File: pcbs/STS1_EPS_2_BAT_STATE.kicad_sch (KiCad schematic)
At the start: 10 parts, among them U4 MIC841H, U5 MIC841L

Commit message: Intermediate commit.
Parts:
- U5: value MIC841L -> MIC841H
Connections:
- net GND: now also U5.2 (GND)
- net GNDREF: no longer U5.2 (GND)
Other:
- note added: "This implements a hysteresis. At BAT_RAW <= 5V, UVLO_SIGNAL is pulled low. If BAT_RAW increases above >= 5,3V, UVLO_SIGNAL is pulled high."
- note removed: "This implements a hysteresis. At BAT_RAW <= 5V, UVLO_SIGNAL is pulled high. If BAT_RAW increases above >= 5,3V, UVLO_SIGNAL is pulled low."
- moved on the sheet: R31, R33, R35, R36, U5

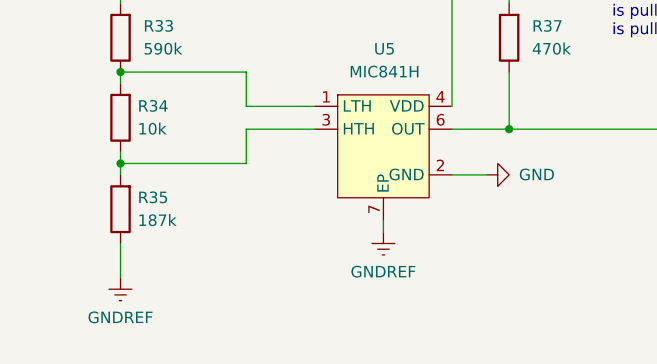
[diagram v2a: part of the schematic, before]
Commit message: Fixed warnings and errors.
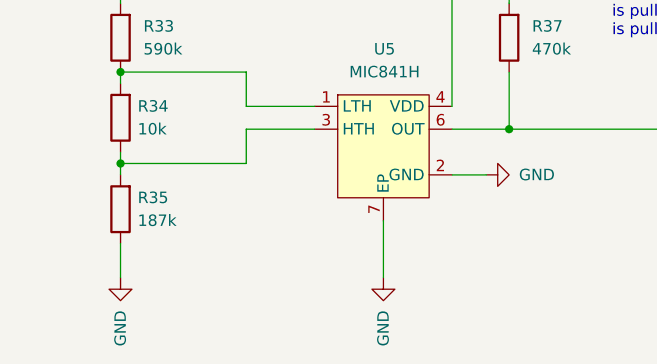
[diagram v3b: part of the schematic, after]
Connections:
- net GNDREF is gone; now on net GND: R35.1, U5.7 (EP)
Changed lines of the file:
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@@
 	(wire
 		(pts
-			(xy 58.42 125.73) (xy 58.42 127)
+			(xy 58.42 125.73) (xy 58.42 132.08)
 		)
 		(stroke
@@
 			)
 			(justify right)
+		)
+	)
+	(symbol
+		(lib_id "power:GND")
+		(at 58.42 132.08 0)
+		(unit 1)
+		(exclude_from_sim no)
+		(in_bom yes)
+		(on_board yes)
+		(dnp no)
+		(property "Reference" "#PWR059"
+			(at 58.42 138.43 0)
+			(effects
+				(font
+					(size 1.27 1.27)
+				)
+				(hide yes)
+			)
+		)
+		(property "Value" "GND"
+			(at 58.42 139.7 90)
+			(effects
+				(font
+					(size 1.27 1.27)
+				)
+				(justify left)
+			)
+		)
+		(property "Footprint" ""
+			(at 58.42 132.08 0)
+			(effects
+				(font
+					(size 1.27 1.27)
+				)
+				(hide yes)
+			)
+		)
+		(property "Datasheet" ""
+			(at 58.42 132.08 0)
+			(effects
+				(font
+					(size 1.27 1.27)
+				)
+				(hide yes)
+			)
+		)
+		(property "Description" "Power symbol creates a global label with name \"GND\" , ground"
+			(at 58.42 132.08 0)
+			(effects
+				(font
+					(size 1.27 1.27)
+				)
+				(hide yes)
+			)
+		)
+		(pin "1"
+		)
+		(instances
+			(project "STS1_EPS_2"
+				(path "/38c03ff7-ea47-4d00-b37d-ddcaa7d87722/f6013889-7b77-4458-9ae4-3903f8947363"
+					(reference "#PWR059")
+					(unit 1)
+				)
+			)
 		)
 	)
@@
 	)
 	(symbol
-		(lib_id "power:GNDREF")
+		(lib_id "power:GND")
 		(at 29.21 132.08 0)
 		(unit 1)
@@
 		(on_board yes)
 		(dnp no)
-		(fields_autoplaced yes)
 		(property "Reference" "#PWR056"
 			(at 29.21 138.43 0)
@@
 			)
 		)
-		(property "Value" "GNDREF"
-			(at 29.21 136.525 0)
-			(effects
-				(font
-					(size 1.27 1.27)
-				)
+		(property "Value" "GND"
+			(at 29.21 139.7 90)
+			(effects
+				(font
+					(size 1.27 1.27)
+				)
+				(justify left)
 			)
 		)
@@
 			)
 		)
-		(property "Description" ""
+		(property "Description" "Power symbol creates a global label with name \"GND\" , ground"
 			(at 29.21 132.08 0)
 			(effects
@@
 					(unit 1)
 				)
-			)
-		)
-	)
-	(symbol
-		(lib_id "power:GNDREF")
-		(at 58.42 127 0)
-		(unit 1)
-		(exclude_from_sim no)
-		(in_bom yes)
-		(on_board yes)
-		(dnp no)
-		(fields_autoplaced yes)
-		(property "Reference" "#PWR059"
-			(at 58.42 133.35 0)
-			(effects
-				(font
-					(size 1.27 1.27)
-				)
-				(hide yes)
-			)
-		)
-		(property "Value" "GNDREF"
-			(at 58.42 131.445 0)
-			(effects
-				(font
-					(size 1.27 1.27)
-				)
-			)
-		)
-		(property "Footprint" ""
-			(at 58.42 127 0)
-			(effects
-				(font
-					(size 1.27 1.27)
-				)
-				(hide yes)
-			)
-		)
-		(property "Datasheet" ""
-			(at 58.42 127 0)
-			(effects
-				(font
-					(size 1.27 1.27)
-				)
-				(hide yes)
-			)
-		)
-		(property "Description" ""
-			(at 58.42 127 0)
-			(effects
-				(font
-					(size 1.27 1.27)
-				)
-				(hide yes)
-			)
-		)
-		(pin "1"
-		)
-		(instances
-			(project "STS1_EPS_2"
-				(path "/38c03ff7-ea47-4d00-b37d-ddcaa7d87722/f6013889-7b77-4458-9ae4-3903f8947363"
-					(reference "#PWR059")
-					(unit 1)
-				)

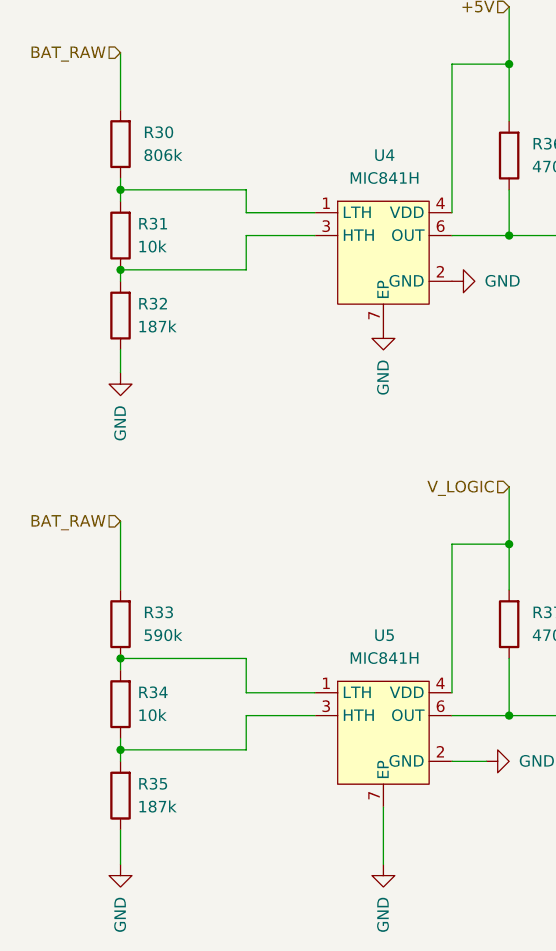
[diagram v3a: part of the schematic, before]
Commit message: Modified some resistor values slightly, so that they fall in common resistor series.
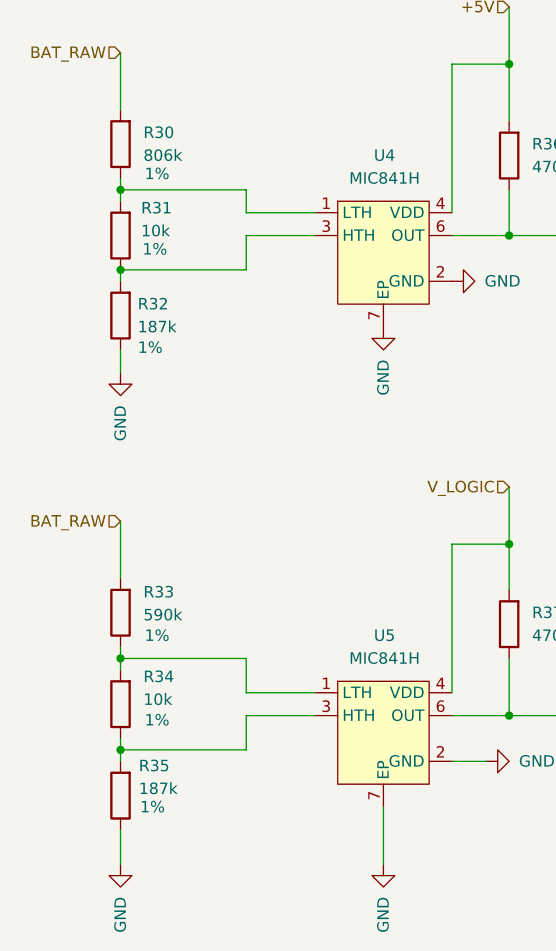
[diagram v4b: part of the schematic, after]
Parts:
- R30, R31, R32, R33, R34, R35: Tolerance (none) -> 1%
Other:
- moved on the sheet: R33
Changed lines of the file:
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@@
+	(wire
+		(pts
+			(xy 29.21 107.95) (xy 29.21 109.22)
+		)
+		(stroke
+			(width 0)
+			(type default)
+		)
+	)
 	(wire
 		(pts
@@
 	(wire
 		(pts
-			(xy 29.21 93.98) (xy 29.21 101.6)
+			(xy 29.21 93.98) (xy 29.21 100.33)
 		)
 		(stroke
@@
 	(symbol
 		(lib_id "Device:R")
-		(at 29.21 105.41 180)
+		(at 29.21 104.14 180)
 		(unit 1)
 		(exclude_from_sim no)
@@
 		(on_board yes)
 		(dnp no)
-		(fields_autoplaced yes)
 		(property "Reference" "R33"
-			(at 31.75 104.1399 0)
+			(at 31.75 101.854 0)
 			(effects
 				(font
@@
 		)
 		(property "Value" "590k"
-			(at 31.75 106.6799 0)
+			(at 31.75 104.394 0)
 			(effects
 				(font
@@
 		)
 		(property "Footprint" "Resistor_SMD:R_0805_2012Metric"
-			(at 30.988 105.41 90)
+			(at 30.988 104.14 90)
 			(effects
 				(font
@@
 		)
 		(property "Datasheet" "~"
-			(at 29.21 105.41 0)
+			(at 29.21 104.14 0)
 			(effects
 				(font
@@
 		)
 		(property "Description" ""
-			(at 29.21 105.41 0)
-			(effects
-				(font
-					(size 1.27 1.27)
-				)
-				(hide yes)
+			(at 29.21 104.14 0)
+			(effects
+				(font
+					(size 1.27 1.27)
+				)
+				(hide yes)
+			)
+		)
+		(property "Tolerance" "1%"
+			(at 33.274 106.68 0)
+			(effects
+				(font
+					(size 1.27 1.27)
+				)
 			)
 		)
@@
 		(on_board yes)
 		(dnp no)
-		(fields_autoplaced yes)
 		(property "Reference" "R31"
-			(at 31.115 60.9599 0)
+			(at 31.496 59.182 0)
 			(effects
 				(font
@@
 		)
 		(property "Value" "10k"
-			(at 31.115 63.4999 0)
+			(at 31.496 61.722 0)
 			(effects
 				(font
@@
 				)
 				(hide yes)
+			)
+		)
+		(property "Tolerance" "1%"
+			(at 33.02 63.754 0)
+			(effects
+				(font
+					(size 1.27 1.27)
+				)
 			)
 		)
@@
 		(on_board yes)
 		(dnp no)
-		(fields_autoplaced yes)
 		(property "Reference" "R32"
 			(at 31.115 69.8499 0)
@@
 				)
 				(hide yes)
+			)
+		)
+		(property "Tolerance" "1%"
+			(at 32.512 74.676 0)
+			(effects
+				(font
+					(size 1.27 1.27)
+				)
 			)
 		)
@@
 		(on_board yes)
 		(dnp no)
-		(fields_autoplaced yes)
 		(property "Reference" "R30"
 			(at 31.75 50.7999 0)
@@
 				)
 				(hide yes)
+			)
+		)
+		(property "Tolerance" "1%"
+			(at 33.274 55.372 0)
+			(effects
+				(font
+					(size 1.27 1.27)
+				)
 			)
 		)
@@
 		(on_board yes)
 		(dnp no)
-		(fields_autoplaced yes)
 		(property "Reference" "R34"
-			(at 31.115 113.0299 0)
+			(at 31.75 111.252 0)
 			(effects
 				(font
@@
 		)
 		(property "Value" "10k"
-			(at 31.115 115.5699 0)
+			(at 31.75 113.792 0)
 			(effects
 				(font
@@
 				)
 				(hide yes)
+			)
+		)
+		(property "Tolerance" "1%"
+			(at 33.274 116.078 0)
+			(effects
+				(font
+					(size 1.27 1.27)
+				)
 			)
 		)
@@
 		(on_board yes)
 		(dnp no)
-		(fields_autoplaced yes)
 		(property "Reference" "R35"
-			(at 31.115 123.1899 0)
+			(at 31.242 121.158 0)
 			(effects
 				(font
@@
 		)
 		(property "Value" "187k"
-			(at 31.115 125.7299 0)
+			(at 31.242 123.698 0)
 			(effects
 				(font
@@
 			)
 		)
+		(property "Tolerance" "1%"
+			(at 32.766 125.73 0)
+			(effects
+				(font
+					(size 1.27 1.27)
+				)
+			)
+		)

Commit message: Added more part numbers.
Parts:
- R30: Part Nr. (none) -> ERA-6AEB8063V
- R31, R34: Part Nr. (none) -> TNPW080510K0FEEA
- R32, R35: Part Nr. (none) -> RN73C2A187KBTDF
- R33: Part Nr. (none) -> TNPW0805590KBEEA
- R36, R37: Part Nr. (none) -> ERA-6AED474V
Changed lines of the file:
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@@
+			)
+		)
+		(property "Part Nr." "TNPW0805590KBEEA"
+			(at 29.21 104.14 0)
+			(effects
+				(font
+					(size 1.27 1.27)
+				)
+				(hide yes)
 			)
 		)
@@
 			)
 		)
+		(property "Part Nr." "TNPW080510K0FEEA"
+			(at 29.21 62.23 0)
+			(effects
+				(font
+					(size 1.27 1.27)
+				)
+				(hide yes)
+			)
+		)
 		(pin "1"
 		)
@@
 			)
 		)
+		(property "Part Nr." "RN73C2A187KBTDF"
+			(at 29.21 71.12 0)
+			(effects
+				(font
+					(size 1.27 1.27)
+				)
+				(hide yes)
+			)
+		)
 		(pin "1"
 		)
@@
 			)
 		)
+		(property "Part Nr." "ERA-6AEB8063V"
+			(at 29.21 52.07 0)
+			(effects
+				(font
+					(size 1.27 1.27)
+				)
+				(hide yes)
+			)
+		)
 		(pin "1"
 		)
@@
 					(size 1.27 1.27)
 				)
+			)
+		)
+		(property "Part Nr." "TNPW080510K0FEEA"
+			(at 29.21 114.3 0)
+			(effects
+				(font
+					(size 1.27 1.27)
+				)
+				(hide yes)
 			)
 		)
@@
 			)
 		)
+		(property "Part Nr." "ERA-6AED474V"
+			(at 72.39 105.41 0)
+			(effects
+				(font
+					(size 1.27 1.27)
+				)
+				(hide yes)
+			)
+		)
 		(pin "1"
 		)
@@
 			)
 		)
+		(property "Part Nr." "ERA-6AED474V"
+			(at 72.39 53.34 0)
+			(effects
+				(font
+					(size 1.27 1.27)
+				)
+				(hide yes)
+			)
+		)
 		(pin "1"
 		)
@@
 			)
 		)
+		(property "Part Nr." ""
+			(at 58.42 111.76 0)
+			(effects
+				(font
+					(size 1.27 1.27)
+				)
+				(hide yes)
+			)
+		)
 		(pin "1"
 		)
@@
 					(size 1.27 1.27)
 				)
+			)
+		)
+		(property "Part Nr." "RN73C2A187KBTDF"
+			(at 29.21 124.46 0)
+			(effects
+				(font
+					(size 1.27 1.27)
+				)
+				(hide yes)
 			)
 		)
@@
 			(at 58.42 58.42 0)
 			(effects
+				(font
+					(size 1.27 1.27)
+				)
+				(hide yes)
+			)
+		)
+		(property "Part Nr." ""
+			(at 58.42 58.42 0)
+			(effects

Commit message: * New symbol for U4 and U5 on STS1_EPS_2. * Made the tracing for U4 and U5 a bit better.
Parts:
- U4, U5: footprint STS_Package_DFN_QFN:TDFN-6 -> Package_TO_SOT_SMD:SOT-353_SC-70-5
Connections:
- net +5V: now also U4.5 (VDD); no longer U4.4 (VDD)
- net EPS_BAT_GOOD: now also U4.4 (OUT); no longer U4.6 (OUT)
- net GND: no longer U4.7 (EP), U5.7 (EP)
- net UVLO_SIGNAL: now also U5.4 (OUT); no longer U5.6 (OUT)
- net V_LOGIC: now also U5.5 (VDD); no longer U5.4 (VDD)
- net at R33.1, R34.2: now also U5.3 (LTH); no longer U5.1 (LTH)
- net at R31.1, R32.2: now also U4.1 (HTH); no longer U4.3 (HTH)
- net at R30.1, R31.2: now also U4.3 (LTH); no longer U4.1 (LTH)
- net at R34.1, R35.2: now also U5.1 (HTH); no longer U5.3 (HTH)
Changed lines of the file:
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@@
-	(wire
-		(pts
-			(xy 58.42 125.73) (xy 58.42 132.08)
-		)
-		(stroke
-			(width 0)
-			(type default)
-		)
-	)
 	(wire
 		(pts
@@
 	)
 	(symbol
-		(lib_id "power:GND")
-		(at 58.42 132.08 0)
-		(unit 1)
-		(exclude_from_sim no)
-		(in_bom yes)
-		(on_board yes)
-		(dnp no)
-		(property "Reference" "#PWR059"
-			(at 58.42 138.43 0)
-			(effects
-				(font
-					(size 1.27 1.27)
-				)
-				(hide yes)
-			)
-		)
-		(property "Value" "GND"
-			(at 58.42 139.7 90)
-			(effects
-				(font
-					(size 1.27 1.27)
-				)
-				(justify left)
-			)
-		)
-		(property "Footprint" ""
-			(at 58.42 132.08 0)
-			(effects
-				(font
-					(size 1.27 1.27)
-				)
-				(hide yes)
-			)
-		)
-		(property "Datasheet" ""
-			(at 58.42 132.08 0)
-			(effects
-				(font
-					(size 1.27 1.27)
-				)
-				(hide yes)
-			)
-		)
-		(property "Description" "Power symbol creates a global label with name \"GND\" , ground"
-			(at 58.42 132.08 0)
-			(effects
-				(font
-					(size 1.27 1.27)
-				)
-				(hide yes)
-			)
-		)
-		(pin "1"
-		)
-		(instances
-			(project "STS1_EPS_2"
-				(path "/38c03ff7-ea47-4d00-b37d-ddcaa7d87722/f6013889-7b77-4458-9ae4-3903f8947363"
-					(reference "#PWR059")
-					(unit 1)
-				)
-			)
-		)
-	)
-	(symbol
 		(lib_id "Device:R")
 		(at 29.21 104.14 180)
@@
 				(path "/38c03ff7-ea47-4d00-b37d-ddcaa7d87722/f6013889-7b77-4458-9ae4-3903f8947363"
 					(reference "R31")
-					(unit 1)
-				)
-			)
-		)
-	)
-	(symbol
-		(lib_id "power:GND")
-		(at 58.42 72.39 0)
-		(unit 1)
-		(exclude_from_sim no)
-		(in_bom yes)
-		(on_board yes)
-		(dnp no)
-		(property "Reference" "#PWR066"
-			(at 58.42 78.74 0)
-			(effects
-				(font
-					(size 1.27 1.27)
-				)
-				(hide yes)
-			)
-		)
-		(property "Value" "GND"
-			(at 58.42 80.01 90)
-			(effects
-				(font
-					(size 1.27 1.27)
-				)
-				(justify left)
-			)
-		)
-		(property "Footprint" ""
-			(at 58.42 72.39 0)
-			(effects
-				(font
-					(size 1.27 1.27)
-				)
-				(hide yes)
-			)
-		)
-		(property "Datasheet" ""
-			(at 58.42 72.39 0)
-			(effects
-				(font
-					(size 1.27 1.27)
-				)
-				(hide yes)
-			)
-		)
-		(property "Description" "Power symbol creates a global label with name \"GND\" , ground"
-			(at 58.42 72.39 0)
-			(effects
-				(font
-					(size 1.27 1.27)
-				)
-				(hide yes)
-			)
-		)
-		(pin "1"
-		)
-		(instances
-			(project "STS1_EPS_2"
-				(path "/38c03ff7-ea47-4d00-b37d-ddcaa7d87722/f6013889-7b77-4458-9ae4-3903f8947363"
-					(reference "#PWR066")
 					(unit 1)
 				)
@@
 			)
 		)
-		(property "Footprint" "STS_Package_DFN_QFN:TDFN-6"
+		(property "Footprint" "Package_TO_SOT_SMD:SOT-353_SC-70-5"
 			(at 58.42 111.76 0)
 			(effects
@@
 		)
 		(pin "5"
-		)
-		(pin "6"
-		)
-		(pin "7"
 		)
 		(instances
@@
 	)
 	(symbol
+		(lib_name "MIC841_1")
 		(lib_id "STS_Analog:MIC841")
 		(at 58.42 58.42 0)
@@
 			)
 		)
-		(property "Footprint" "STS_Package_DFN_QFN:TDFN-6"
+		(property "Footprint" "Package_TO_SOT_SMD:SOT-353_SC-70-5"
 			(at 58.42 58.42 0)
 			(effects
@@
 		(pin "5"
 		)
-		(pin "6"
-		)
-		(pin "7"
-		)
 		(instances

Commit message: * Cell balancer is now deactivated by UVLO signal, rather than bat fault signal * Bat Fault signal is now an open drain output
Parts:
- U4: value MIC841H -> MIC841N
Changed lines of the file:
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@@
 			)
 		)
-		(property "Value" "MIC841H"
+		(property "Value" "MIC841N"
 			(at 58.547 55.88 0)
 			(effects

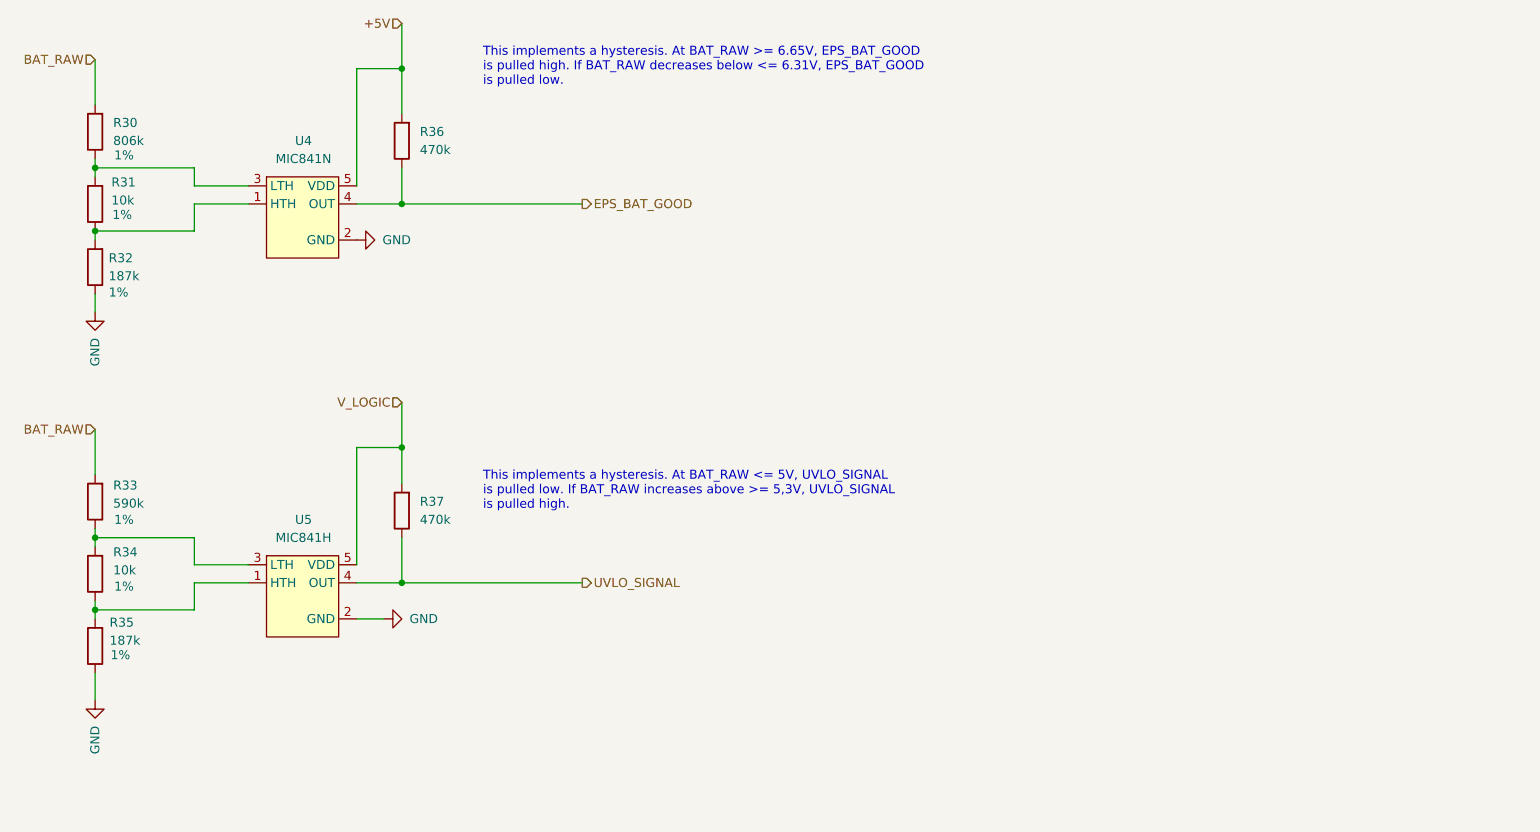
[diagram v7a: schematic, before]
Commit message: feat(EPS PCB 2): start redesign & cleanup for less idle power consumption
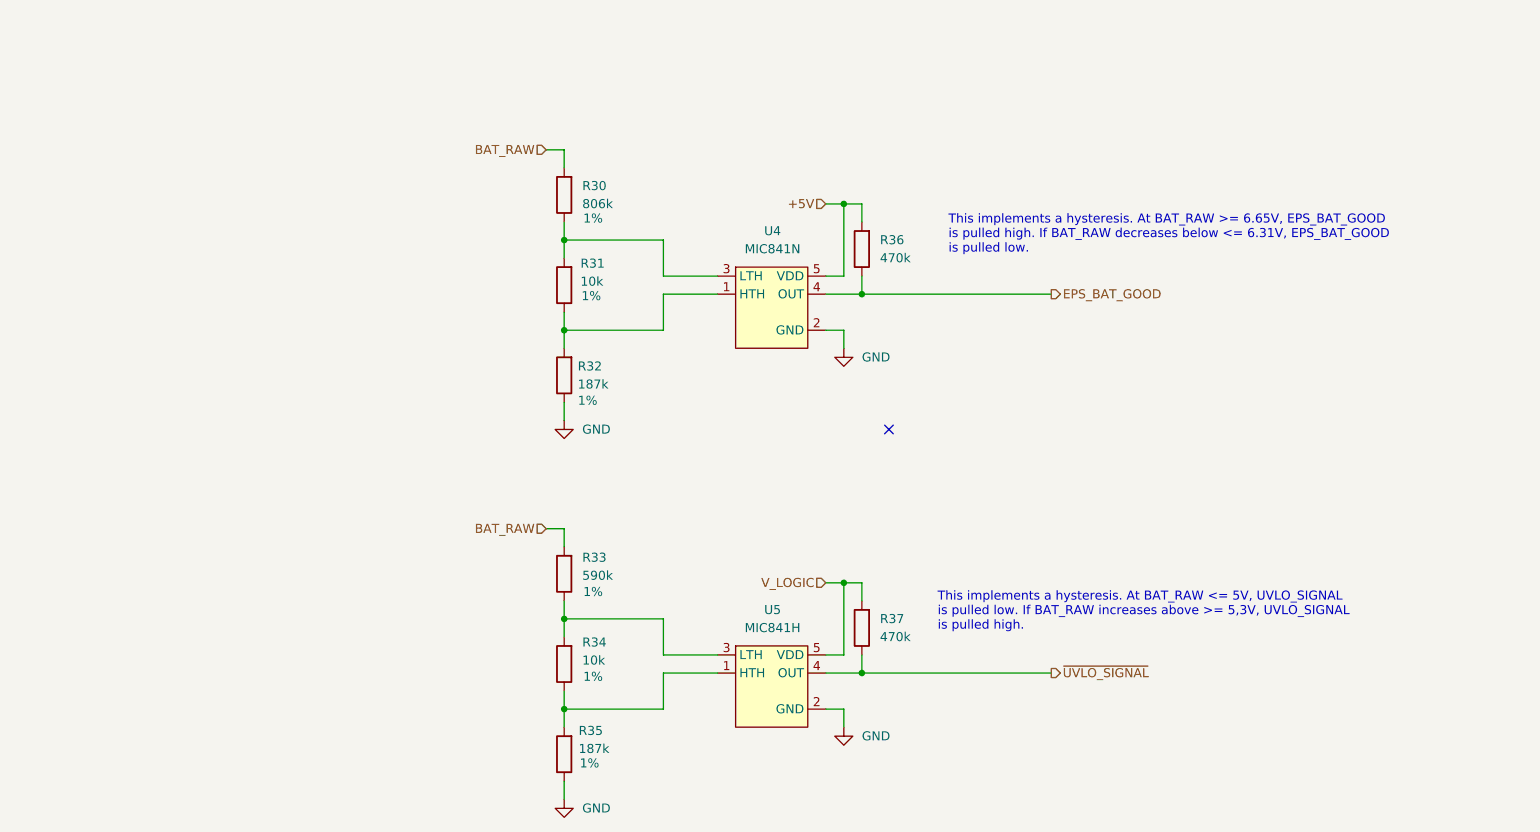
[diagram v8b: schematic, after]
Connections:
- net UVLO_SIGNAL renamed ~{UVLO_SIGNAL}
- no-connect marks 0 -> 1
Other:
- moved on the sheet: R30, R31, R32, R33, R34, R35, R36, R37, U4, U5
